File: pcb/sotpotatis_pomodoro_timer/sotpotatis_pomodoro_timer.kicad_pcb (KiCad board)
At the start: 4 copper layers, 81.1 x 58.7 mm, 48 parts, among them J2 USB_C_PWR_IN, SW1 LEFT_BTN, SW2 PRESET_1_BTN, SW3 PRESET_2_BTN, SW4 PRESET_3_BTN, SW5 RIGHT_BTN, SW6 PWR_SWITCH, U1 ATtiny84A-P

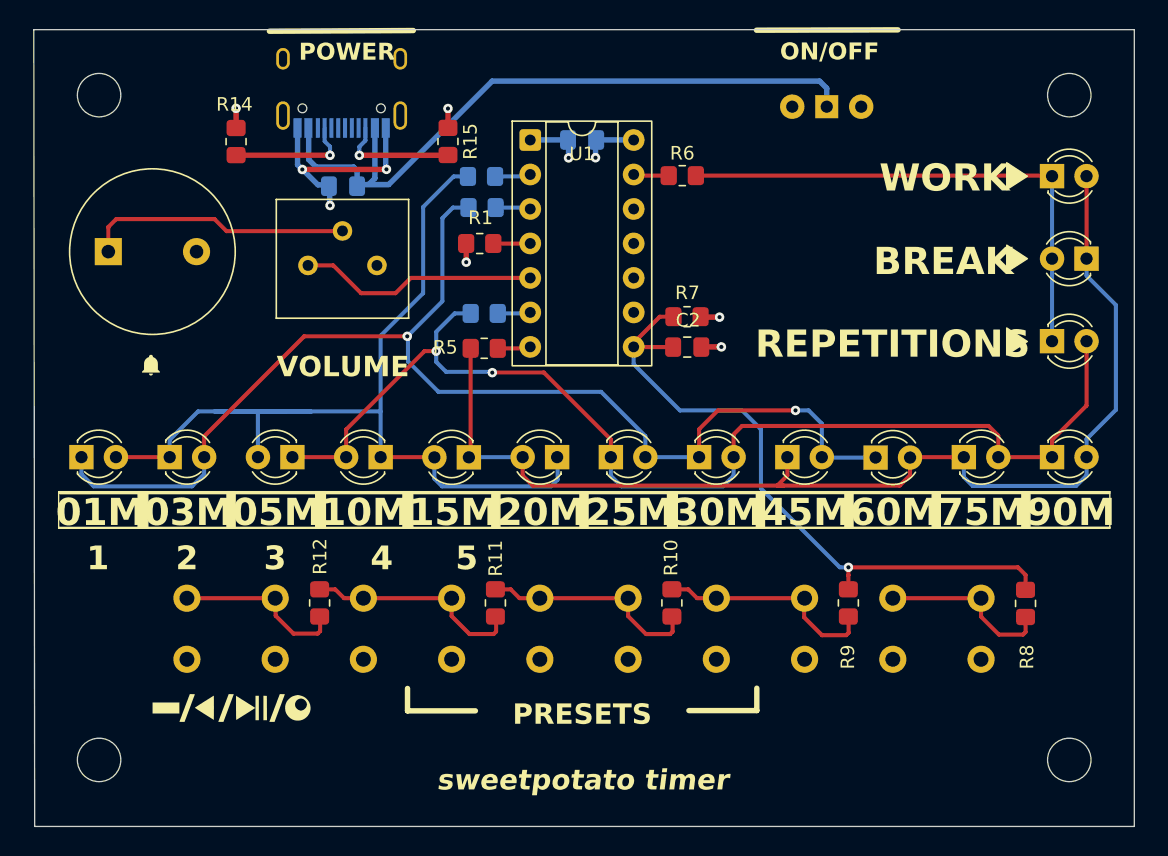
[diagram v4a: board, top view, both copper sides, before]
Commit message: fix: Some silkscreen labels positioned wrong + round off board edge
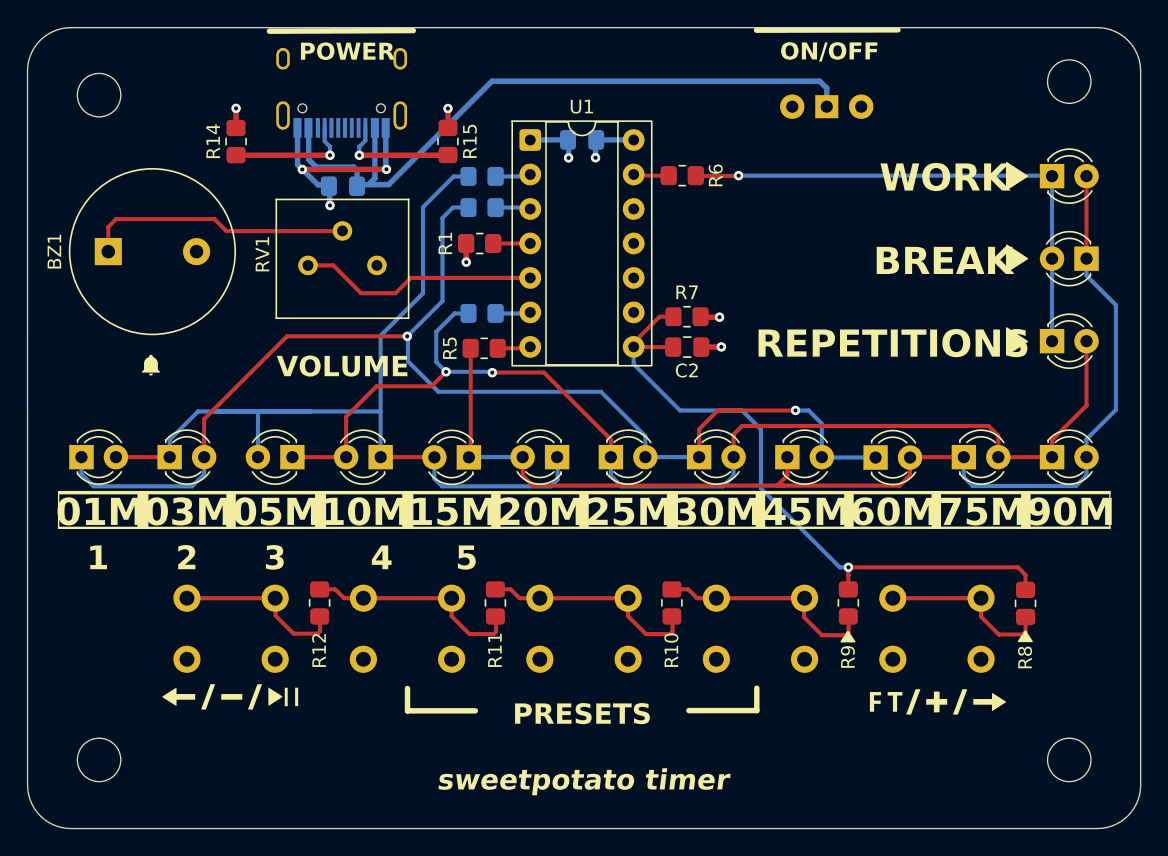
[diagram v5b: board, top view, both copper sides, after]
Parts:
- removed LB1: LOGO, LOGO
- added G***: LOGO, LOGO, F.Cu at (158.0, 92.5)
- added G***: LOGO, LOGO, F.Cu at (106.1, 92.1)
- moved H2 1.00 mm to (167.8, 46.8)
- moved R4 0.16 mm to (124.5, 63.9)
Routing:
- net Net-(D1-K): track 89.5 -> 90.3 mm
- net Net-(D11-A): track 86.0 -> 86.7 mm
- net Net-(D13-K): vias 0 -> 1
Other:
- board size 81.1 x 58.7 mm -> 82 x 59 mm

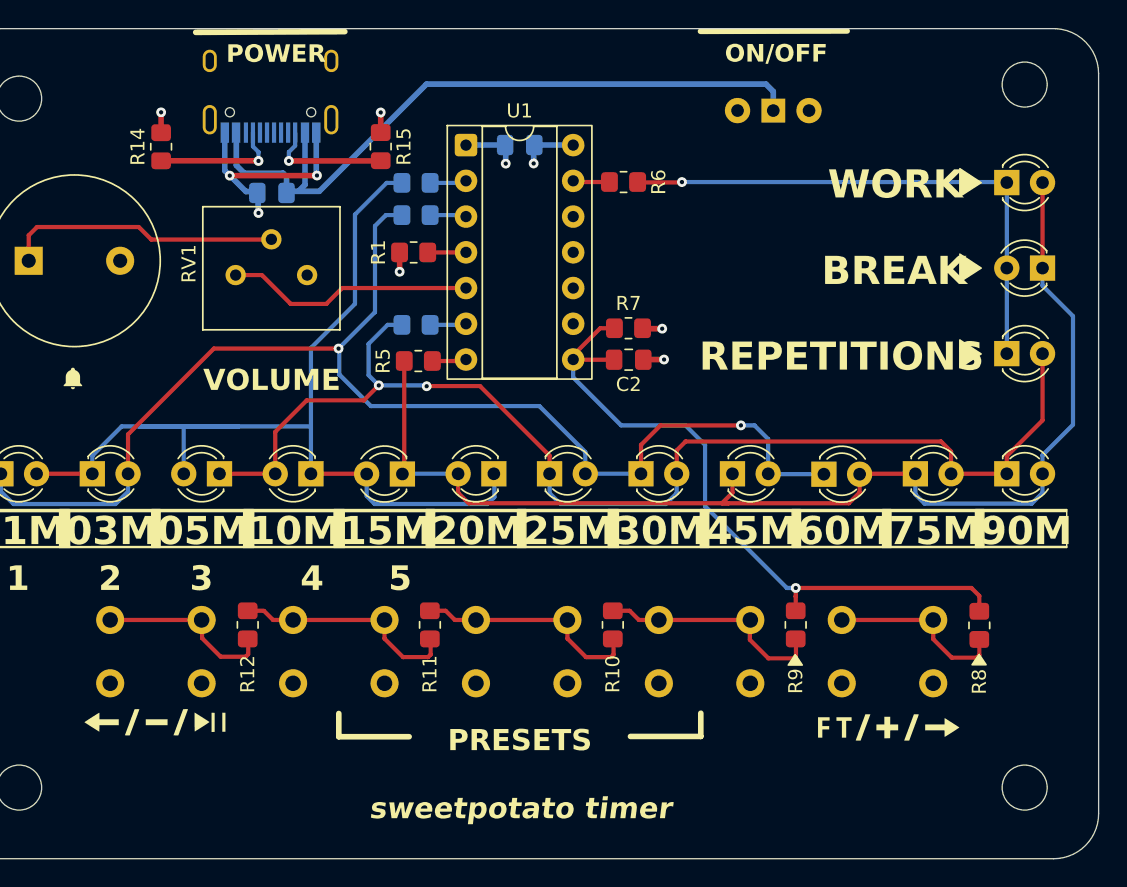
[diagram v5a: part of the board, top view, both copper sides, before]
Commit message: fix: All silkscreen labels except the logo is now exactly where they should for prod.
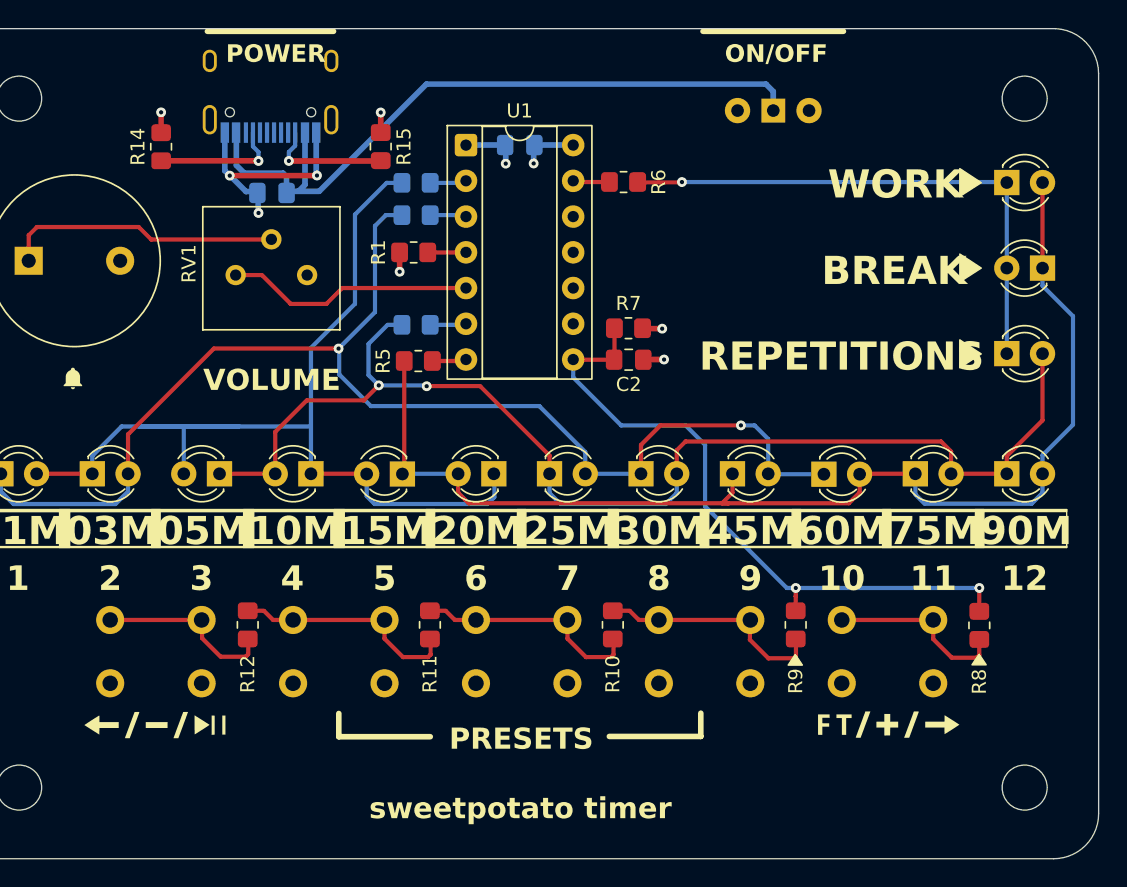
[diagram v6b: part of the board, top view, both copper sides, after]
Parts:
- moved H2 1.00 mm to (167.8, 47.8)
- moved G*** 0.20 mm to (158.0, 92.3)
- moved G*** 0.20 mm to (106.1, 92.3)
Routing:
- net PA5: track 48.5 -> 47.4 mm, vias 1 -> 2
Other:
- board text added: "10"
- board text added: "11"
- board text added: "12"
- board text added: "6"
- board text added: "7"
- board text added: "8"
- board text added: "9"
- board text added: "rev 1.0.0 - ${CURRENT_DATE}"

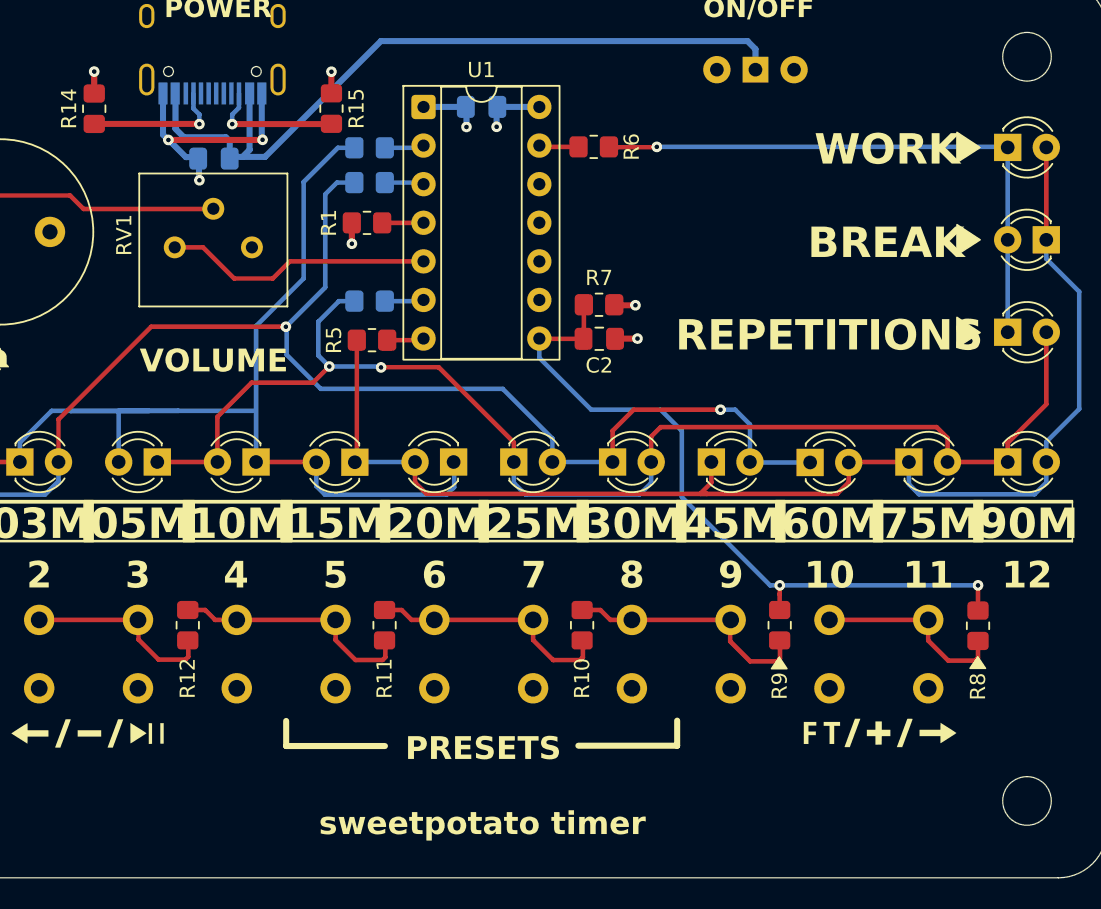
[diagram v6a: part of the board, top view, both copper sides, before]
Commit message: fix: Small changes to silkscreen & component placement to make board look clearer
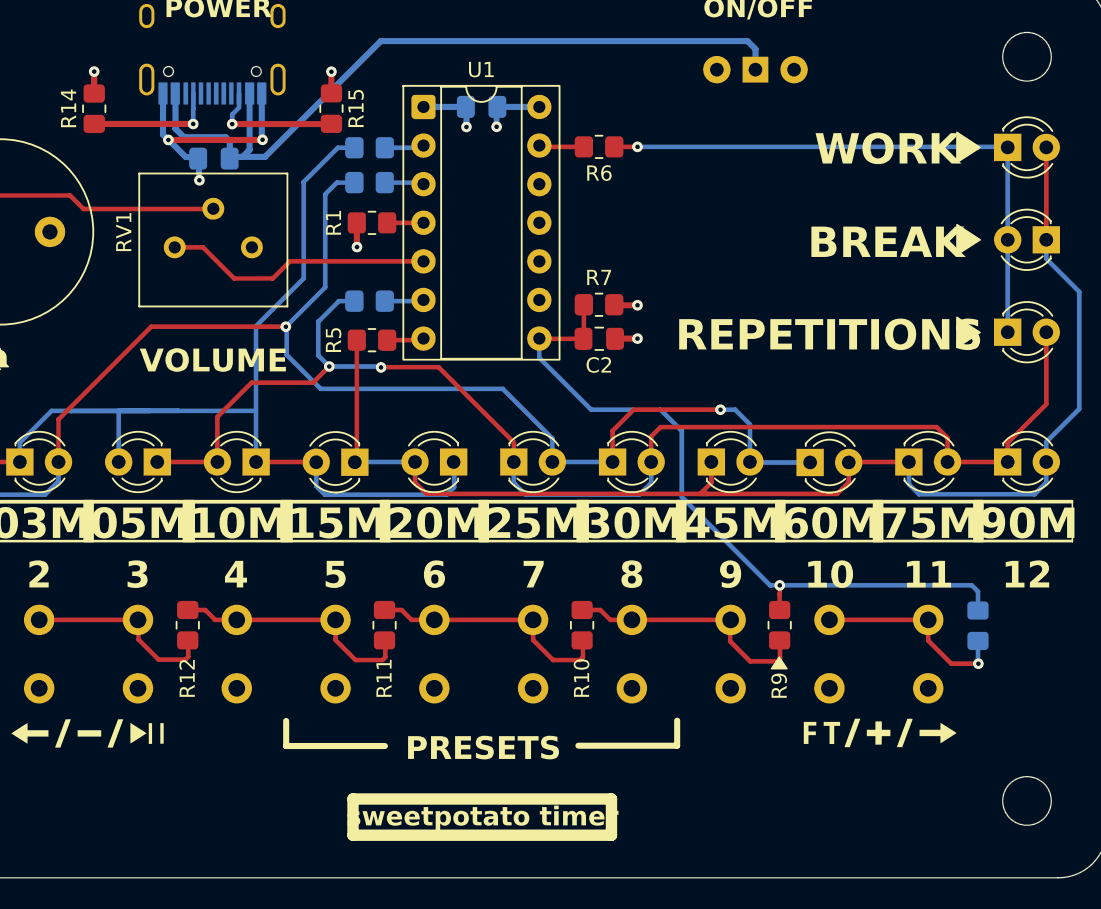
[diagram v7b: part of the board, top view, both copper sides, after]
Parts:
- R8: moved to B.Cu
- moved R6 0.35 mm to (139.6, 53.7)
- moved R1 0.33 mm to (124.7, 58.7)
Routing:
- net PA5: track 47.4 -> 47.1 mm, vias 2 -> 1
- net Net-(R8-Pad1): track 13.5 -> 13.3 mm, vias 0 -> 1
